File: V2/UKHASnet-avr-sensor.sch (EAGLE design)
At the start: 31 parts, among them J1 AVR_SPI_PRG_62X3_LOCK, U1 MCP1700-3302E/TO, U2 ATMEGA328P-PU, X1 SMA-142-0711-881/886, Y1 RESONATORPTH

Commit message: Tweaks.
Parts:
- added JP15: M01PTH, SparkFun-Connectors:M01PTH
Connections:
- net VCC: now also JP15.1
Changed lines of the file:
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@@
 <part name="JP10" library="SparkFun-Connectors" deviceset="M01" device="PTH"/>
 <part name="JP11" library="SparkFun-Connectors" deviceset="M01" device="PTH"/>
+<part name="JP15" library="SparkFun-Connectors" deviceset="M01" device="PTH"/>
 </parts>
 <sheets>
@@
 <instance part="JP10" gate="G$1" x="144.78" y="-7.62" rot="R180"/>
 <instance part="JP11" gate="G$1" x="-48.26" y="25.4"/>
+<instance part="JP15" gate="G$1" x="144.78" y="83.82" rot="R180"/>
 </instances>
 <busses>
@@
 <label x="63.5" y="7.62" size="1.778" layer="95"/>
 </segment>
+<segment>
+<pinref part="JP15" gate="G$1" pin="1"/>
+<wire x1="137.16" y1="83.82" x2="127" y2="83.82" width="0.1524" layer="91"/>
+<label x="129.54" y="83.82" size="1.778" layer="95"/>
+</segment>
 </net>

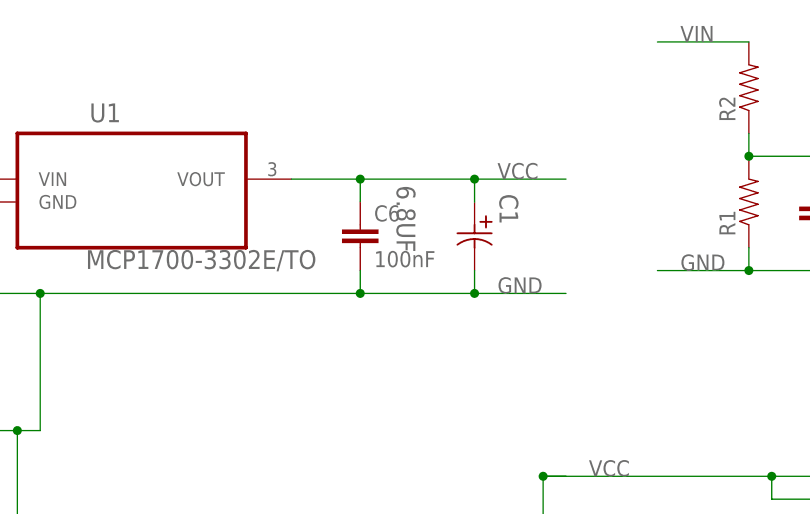
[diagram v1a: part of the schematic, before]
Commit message: Correct cap calue.
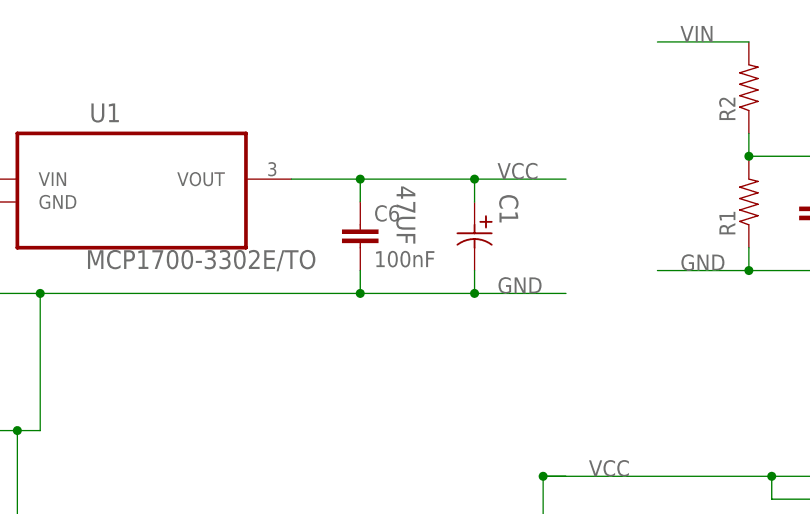
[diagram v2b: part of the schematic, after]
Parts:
- C1: value 6.8UF -> 47UF
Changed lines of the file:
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@@
 <part name="R2" library="SparkFun" deviceset="RESISTOR" device="PTH-1/4W"/>
 <part name="R3" library="SparkFun" deviceset="RESISTOR" device="PTH-1/4W"/>
-<part name="C1" library="1000ufCap" deviceset="EEU" device="-P1.5" technology="FC1J6R8" value="6.8UF"/>
+<part name="C1" library="1000ufCap" deviceset="EEU" device="-P1.5" technology="FC1J6R8" value="47UF"/>
 <part name="R4" library="SparkFun" deviceset="RESISTOR" device="PTH-1/4W"/>
 <part name="Y1" library="SparkFun" deviceset="RESONATOR" device="PTH"/>

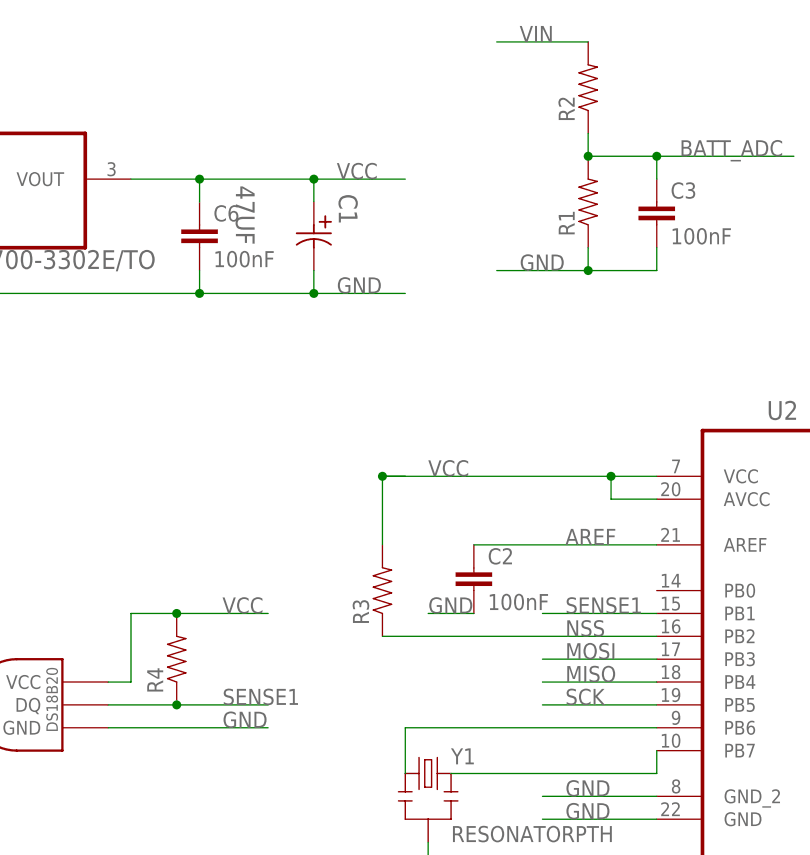
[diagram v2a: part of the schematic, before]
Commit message: Add resistor values.
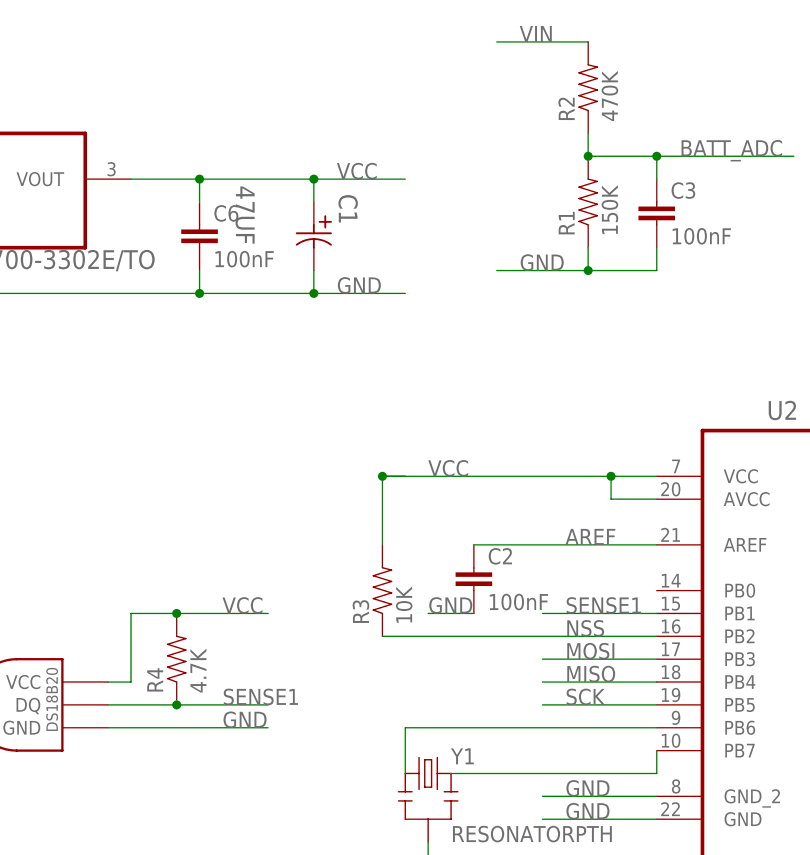
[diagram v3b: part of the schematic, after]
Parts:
- R1: value (none) -> 150K
- R2: value (none) -> 470K
- R3: value (none) -> 10K
- R4: value (none) -> 4.7K
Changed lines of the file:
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@@
 <part name="U1" library="mcp1700" deviceset="MCP1700-3302E/TO" device=""/>
 <part name="JP9" library="SparkFun-Connectors" deviceset="M01" device="PTH"/>
-<part name="R1" library="SparkFun" deviceset="RESISTOR" device="PTH-1/4W"/>
-<part name="R2" library="SparkFun" deviceset="RESISTOR" device="PTH-1/4W"/>
-<part name="R3" library="SparkFun" deviceset="RESISTOR" device="PTH-1/4W"/>
+<part name="R1" library="SparkFun" deviceset="RESISTOR" device="PTH-1/4W" value="150K"/>
+<part name="R2" library="SparkFun" deviceset="RESISTOR" device="PTH-1/4W" value="470K"/>
+<part name="R3" library="SparkFun" deviceset="RESISTOR" device="PTH-1/4W" value="10K"/>
 <part name="C1" library="1000ufCap" deviceset="EEU" device="-P1.5" technology="FC1J6R8" value="47UF"/>
-<part name="R4" library="SparkFun" deviceset="RESISTOR" device="PTH-1/4W"/>
+<part name="R4" library="SparkFun" deviceset="RESISTOR" device="PTH-1/4W" value="4.7K"/>
 <part name="Y1" library="SparkFun" deviceset="RESONATOR" device="PTH"/>
 <part name="JP12" library="SparkFun-Connectors" deviceset="M01" device="PTH"/>

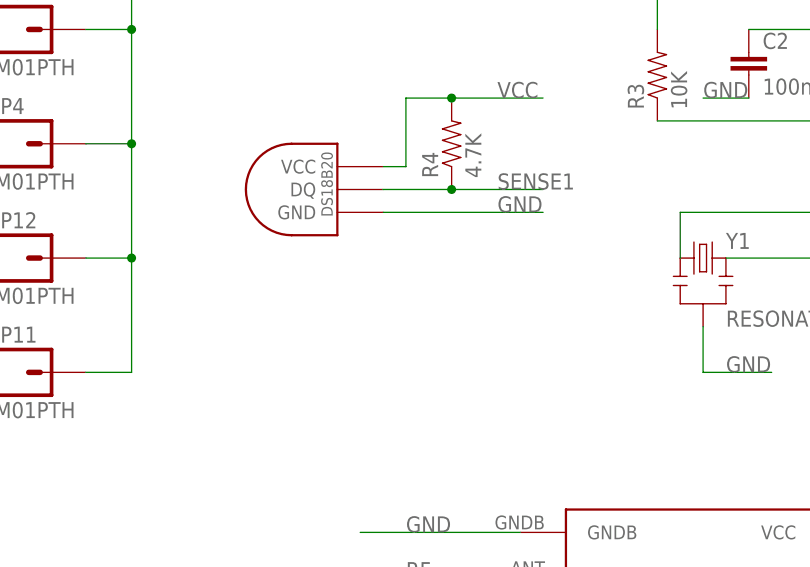
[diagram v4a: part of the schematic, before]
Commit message: Add extra pad for dht22.
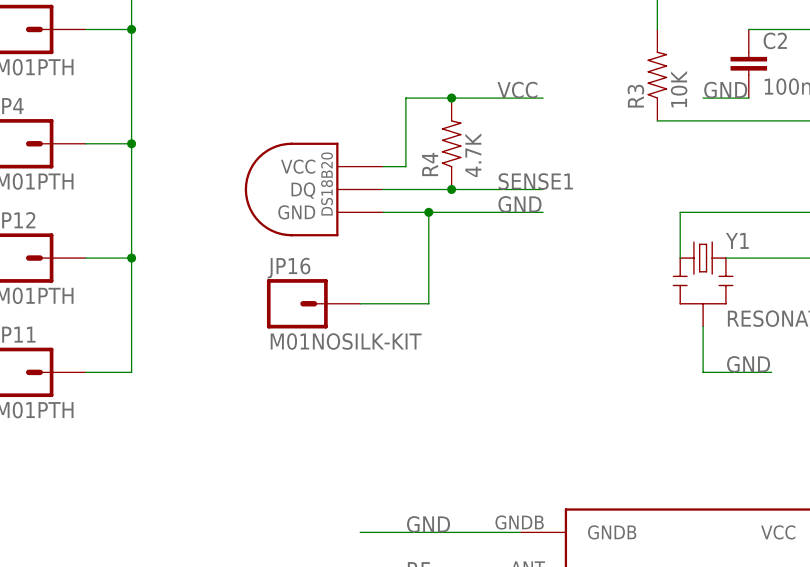
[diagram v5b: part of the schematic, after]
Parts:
- added JP16: M01NOSILK-KIT, SparkFun-Connectors:M01NOSILK-KIT
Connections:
- net GND: now also JP16.1
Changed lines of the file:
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@@
 <layer number="54" name="bGND_GNDA" color="1" fill="9" visible="no" active="no"/>
 <layer number="56" name="wert" color="7" fill="1" visible="no" active="no"/>
+<layer number="57" name="tCAD" color="7" fill="1" visible="no" active="no"/>
 <layer number="91" name="Nets" color="2" fill="1" visible="yes" active="yes"/>
 <layer number="92" name="Busses" color="1" fill="1" visible="yes" active="yes"/>
@@
 <layer number="97" name="Info" color="7" fill="1" visible="yes" active="yes"/>
 <layer number="98" name="Guide" color="6" fill="1" visible="yes" active="yes"/>
+<layer number="99" name="SpiceOrder" color="7" fill="1" visible="yes" active="yes"/>
 <layer number="100" name="Muster" color="7" fill="1" visible="no" active="no"/>
 <layer number="101" name="Patch_Top" color="12" fill="4" visible="yes" active="yes"/>
@@
 <layer number="109" name="fp9" color="7" fill="1" visible="yes" active="yes"/>
 <layer number="110" name="fp0" color="7" fill="1" visible="yes" active="yes"/>
+<layer number="111" name="LPC17xx" color="7" fill="1" visible="no" active="yes"/>
+<layer number="112" name="tSilk" color="7" fill="1" visible="no" active="yes"/>
+<layer number="113" name="IDFDebug" color="4" fill="1" visible="no" active="yes"/>
 <layer number="116" name="Patch_BOT" color="9" fill="4" visible="yes" active="yes"/>
 <layer number="121" name="_tsilk" color="7" fill="1" visible="yes" active="yes"/>
@@
 <layer number="124" name="bTestmark" color="7" fill="1" visible="yes" active="yes"/>
 <layer number="125" name="_tNames" color="7" fill="1" visible="yes" active="yes"/>
+<layer number="126" name="_bNames" color="7" fill="1" visible="no" active="yes"/>
+<layer number="127" name="_tValues" color="7" fill="1" visible="no" active="yes"/>
+<layer number="128" name="_bValues" color="7" fill="1" visible="no" active="yes"/>
 <layer number="131" name="tAdjust" color="7" fill="1" visible="yes" active="yes"/>
 <layer number="132" name="bAdjust" color="7" fill="1" visible="yes" active="yes"/>
 <layer number="144" name="Drill_legend" color="7" fill="1" visible="yes" active="yes"/>
+<layer number="150" name="Notes" color="7" fill="1" visible="no" active="yes"/>
 <layer number="151" name="HeatSink" color="7" fill="1" visible="yes" active="yes"/>
+<layer number="152" name="_bDocu" color="7" fill="1" visible="no" active="yes"/>
+<layer number="153" name="FabDoc1" color="7" fill="1" visible="no" active="yes"/>
+<layer number="154" name="FabDoc2" color="7" fill="1" visible="no" active="yes"/>
+<layer number="155" name="FabDoc3" color="7" fill="1" visible="no" active="yes"/>
 <layer number="199" name="Contour" color="7" fill="1" visible="yes" active="yes"/>
 <layer number="200" name="200bmp" color="1" fill="10" visible="no" active="no"/>
@@
 <layer number="223" name="223bmp" color="24" fill="1" visible="no" active="no"/>
 <layer number="224" name="224bmp" color="25" fill="1" visible="no" active="no"/>
+<layer number="248" name="Housing" color="7" fill="1" visible="no" active="yes"/>
+<layer number="249" name="Edge" color="7" fill="1" visible="no" active="yes"/>
 <layer number="250" name="Descript" color="3" fill="1" visible="no" active="no"/>
 <layer number="251" name="SMDround" color="12" fill="11" visible="no" active="no"/>
@@
 <part name="JP11" library="SparkFun-Connectors" deviceset="M01" device="PTH"/>
 <part name="JP15" library="SparkFun-Connectors" deviceset="M01" device="PTH"/>
+<part name="JP16" library="SparkFun-Connectors" deviceset="M01" device="NOSILK-KIT"/>
 </parts>
 <sheets>
@@
 <instance part="JP11" gate="G$1" x="-48.26" y="25.4"/>
 <instance part="JP15" gate="G$1" x="144.78" y="83.82" rot="R180"/>
+<instance part="JP16" gate="G$1" x="-17.78" y="33.02"/>
 </instances>
 <busses>
@@
 <segment>
 <pinref part="U$2" gate="G$1" pin="GND"/>
-<wire x1="-7.62" y1="43.18" x2="10.16" y2="43.18" width="0.1524" layer="91"/>
+<wire x1="-7.62" y1="43.18" x2="-2.54" y2="43.18" width="0.1524" layer="91"/>
 <label x="5.08" y="43.18" size="1.778" layer="95"/>
-</segment>
-<segment>
+<pinref part="JP16" gate="G$1" pin="1"/>
+<wire x1="-2.54" y1="43.18" x2="10.16" y2="43.18" width="0.1524" layer="91"/>
+<wire x1="-10.16" y1="33.02" x2="-2.54" y2="33.02" width="0.1524" layer="91"/>
+<wire x1="-2.54" y1="33.02" x2="-2.54" y2="43.18" width="0.1524" layer="91"/>
+<junction x="-2.54" y="43.18"/>
+</segment>
+<segment>

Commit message: Fix dht22 pad.
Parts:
- removed JP16: M01NOSILK-KIT, SparkFun-Connectors:M01NOSILK-KIT
- added PAD1: WIREPAD1,6/0,9, wirepad:WIREPAD1,6/0,9
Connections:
- net GND: now also PAD1.P; no longer JP16.1
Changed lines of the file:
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@@
 <part name="JP11" library="SparkFun-Connectors" deviceset="M01" device="PTH"/>
 <part name="JP15" library="SparkFun-Connectors" deviceset="M01" device="PTH"/>
-<part name="JP16" library="SparkFun-Connectors" deviceset="M01" device="NOSILK-KIT"/>
+<part name="PAD1" library="wirepad" deviceset="WIREPAD" device="1,6/0,9"/>
 </parts>
 <sheets>
@@
 <instance part="JP11" gate="G$1" x="-48.26" y="25.4"/>
 <instance part="JP15" gate="G$1" x="144.78" y="83.82" rot="R180"/>
-<instance part="JP16" gate="G$1" x="-17.78" y="33.02"/>
+<instance part="PAD1" gate="G$1" x="-15.24" y="33.02"/>
 </instances>
 <busses>
@@
 <wire x1="-7.62" y1="43.18" x2="-2.54" y2="43.18" width="0.1524" layer="91"/>
 <label x="5.08" y="43.18" size="1.778" layer="95"/>
-<pinref part="JP16" gate="G$1" pin="1"/>
 <wire x1="-2.54" y1="43.18" x2="10.16" y2="43.18" width="0.1524" layer="91"/>
-<wire x1="-10.16" y1="33.02" x2="-2.54" y2="33.02" width="0.1524" layer="91"/>
+<wire x1="-12.7" y1="33.02" x2="-2.54" y2="33.02" width="0.1524" layer="91"/>
 <wire x1="-2.54" y1="33.02" x2="-2.54" y2="43.18" width="0.1524" layer="91"/>
 <junction x="-2.54" y="43.18"/>
-</segment>
-<segment>
+<pinref part="PAD1" gate="G$1" pin="P"/>
+</segment>
+<segment>
